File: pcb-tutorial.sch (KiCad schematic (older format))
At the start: 14 parts

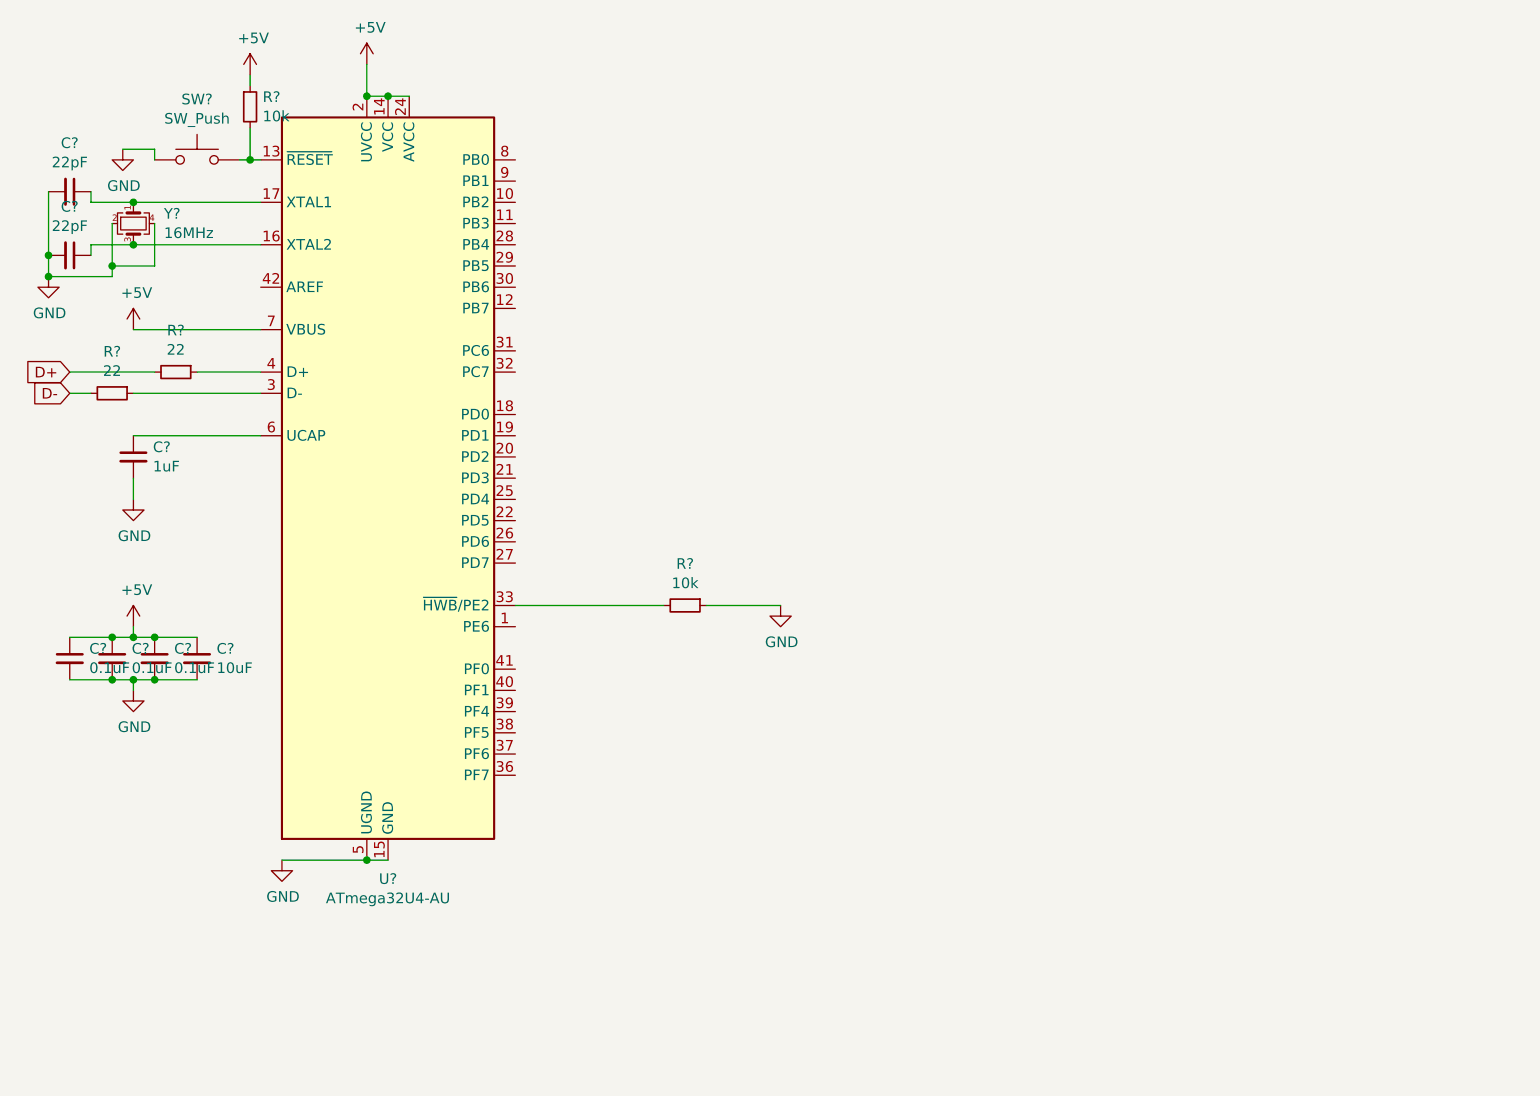
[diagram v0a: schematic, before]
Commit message: completed pcb binding
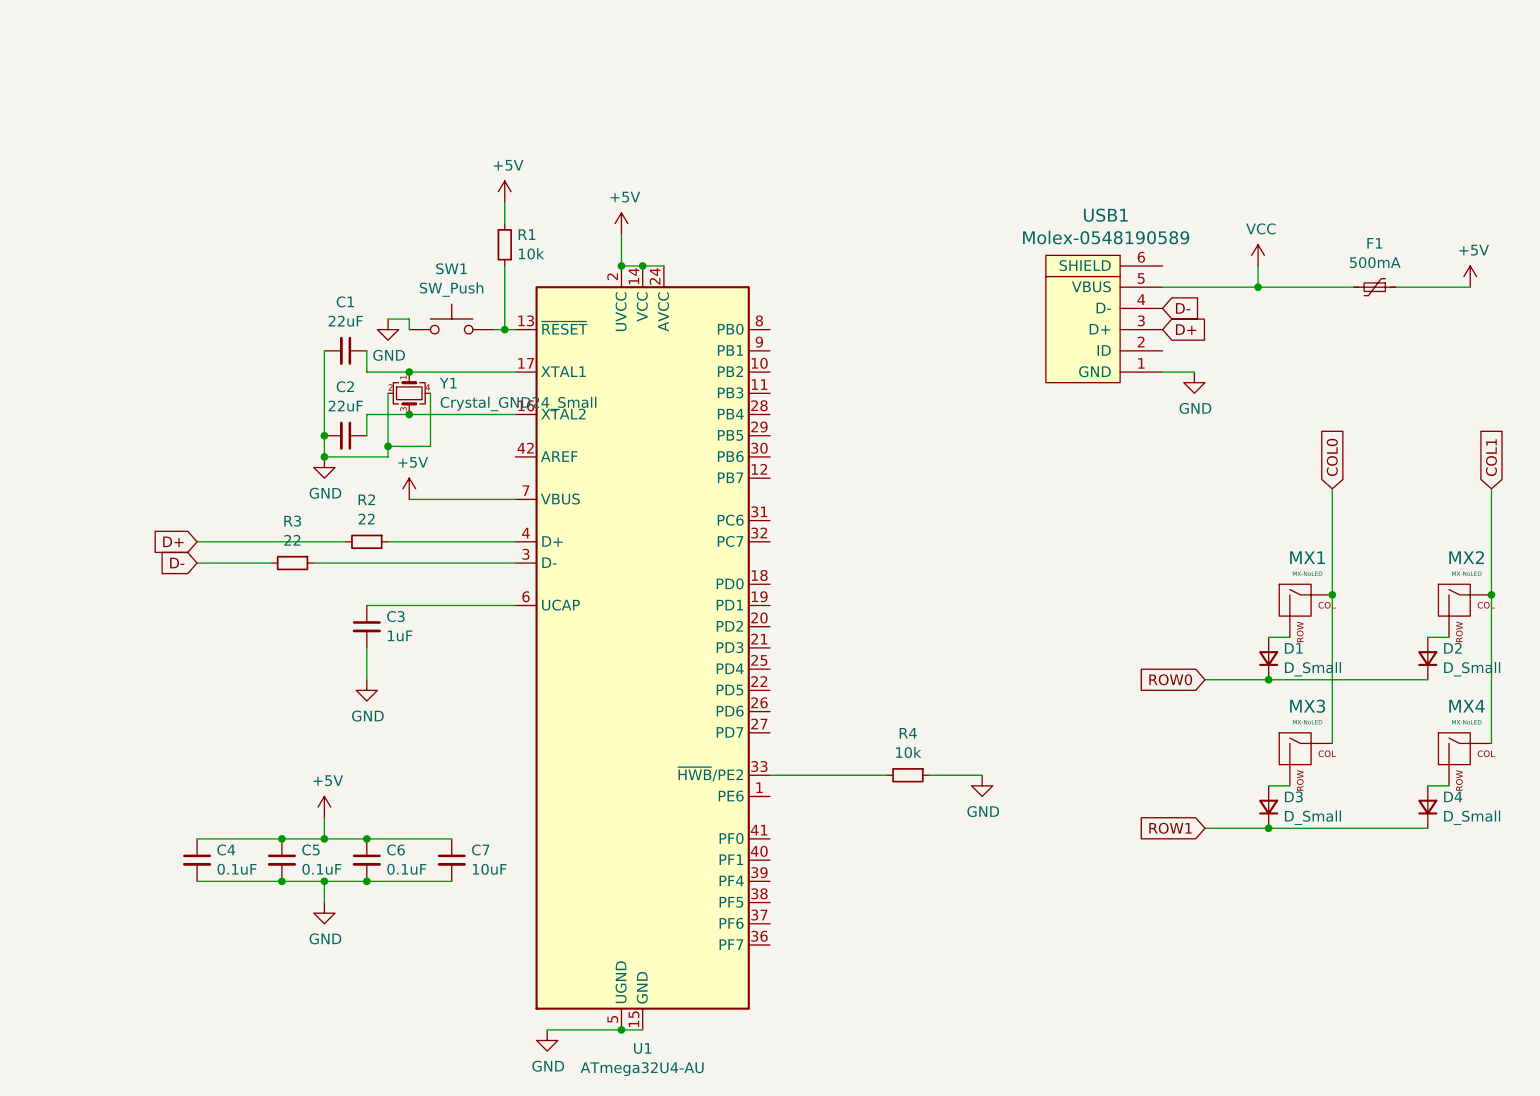
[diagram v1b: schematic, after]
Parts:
- removed C?: 1uF, symbol Device:C_Small
- removed C? (x3): 0.1uF, symbol Device:C_Small
- removed C?: 10uF, symbol Device:C_Small
- removed C? (x2): 22pF, symbol Device:C_Small
- removed R? (x2): 10k, symbol Device:R_Small
- removed R? (x2): 22, symbol Device:R_Small
- removed SW?: SW_Push, symbol Switch:SW_Push
- removed U?: ATmega32U4-AU, Package_QFP:TQFP-44_10x10mm_P0.8mm, symbol MCU_Microchip_ATmega:ATmega32U4-AU
- removed Y?: 16MHz, symbol Device:Crystal_GND24_Small
- added C1, C2: 22uF, Capacitor_SMD:C_0805_2012Metric, symbol Device:C_Small
- added C3: 1uF, Capacitor_SMD:C_0805_2012Metric, symbol Device:C_Small
- added C4, C5, C6: 0.1uF, Capacitor_SMD:C_0805_2012Metric, symbol Device:C_Small
- added C7: 10uF, Capacitor_SMD:C_0805_2012Metric, symbol Device:C_Small
- added D1, D2, D3, D4: D_Small, Diode_SMD:D_SOD-123, symbol Device:D_Small
- added F1: 500mA, Fuse:Fuse_1206_3216Metric, symbol Device:Polyfuse_Small
- added MX1, MX2, MX3, MX4: MX-NoLED, MX_Alps_Hybrid:MX-1U-NoLED, symbol MX_Alps_Hybrid:MX-NoLED
- added R1, R4: 10k, Resistor_SMD:R_0805_2012Metric, symbol Device:R_Small
- added R2, R3: 22, Resistor_SMD:R_0805_2012Metric, symbol Device:R_Small
- added SW1: SW_Push, random-keyboard-parts:SKQG-1155865, symbol Switch:SW_Push
- added U1: ATmega32U4-AU, Package_QFP:TQFP-44_10x10mm_P0.8mm, symbol MCU_Microchip_ATmega:ATmega32U4-AU
- added USB1: Molex-0548190589, random-keyboard-parts:Molex-0548190589, symbol random-keyboard-parts:Molex-0548190589
- added Y1: Crystal_GND24_Small, Crystal:Crystal_SMD_3225-4Pin_3.2x2.5mm, symbol Device:Crystal_GND24_Small
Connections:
- net +5V: now also C4.1, C5.1, C6.1, C7.1, F1.1, R1.2, U1.14 (VCC), U1.2 (UVCC), U1.24 (AVCC), U1.34 (VCC), U1.44 (AVCC), U1.7 (VBUS)
- net D+: now also R2.2, USB1.3 (D+)
- net D-: now also R3.2, USB1.4 (D-)
- net GND: now also C1.2, C2.2, C3.2, C4.2, C5.2, C6.2, C7.2, R4.1, SW1.1, U1.15 (GND), U1.23 (GND), U1.35 (GND), U1.43 (GND), U1.5 (UGND), USB1.1 (GND), Y1.2, Y1.4
- new net: R1.1, SW1.2, U1.13 (~RESET)
- new net: C2.1, U1.16 (XTAL2), Y1.3
- new net: C1.1, U1.17 (XTAL1), Y1.1
- new net: R3.1, U1.3 (D-)
- new net: R4.2, U1.33 (~HWB~/PE2)
- new net: R2.1, U1.4 (D+)
- new net: C3.1, U1.6 (UCAP)
- new net: D1.2 (A), MX1.2 (ROW)
- new net: D2.2 (A), MX2.2 (ROW)
- new net: D3.2 (A), MX3.2 (ROW)
- new net: D4.2 (A), MX4.2 (ROW)
- new net COL0: MX1.1 (COL), MX3.1 (COL)
- new net COL1: MX2.1 (COL), MX4.1 (COL)
- new net ROW0: D1.1 (K), D2.1 (K)
- new net ROW1: D3.1 (K), D4.1 (K)
- new net VCC: F1.2, USB1.5 (VBUS)

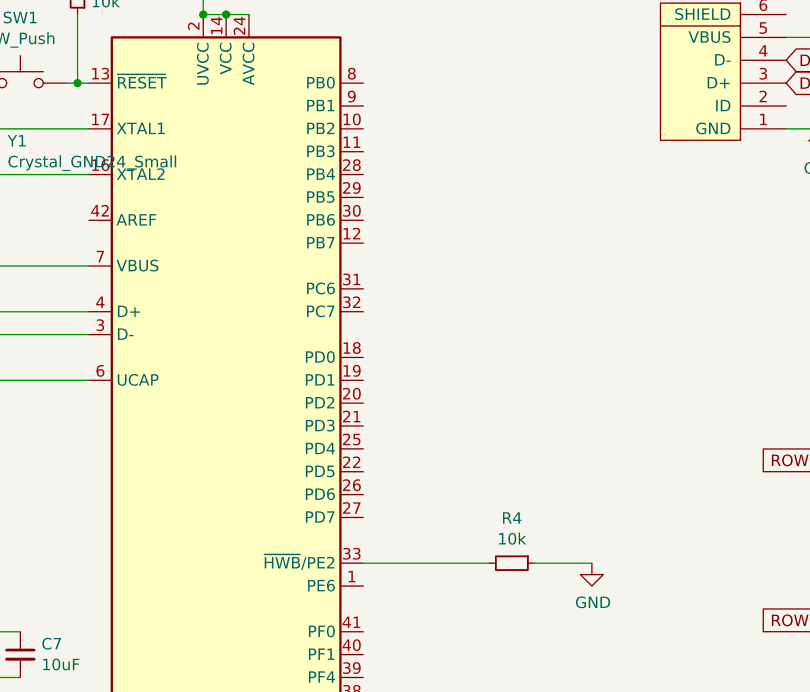
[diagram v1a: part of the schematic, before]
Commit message: Completed PCB Routing
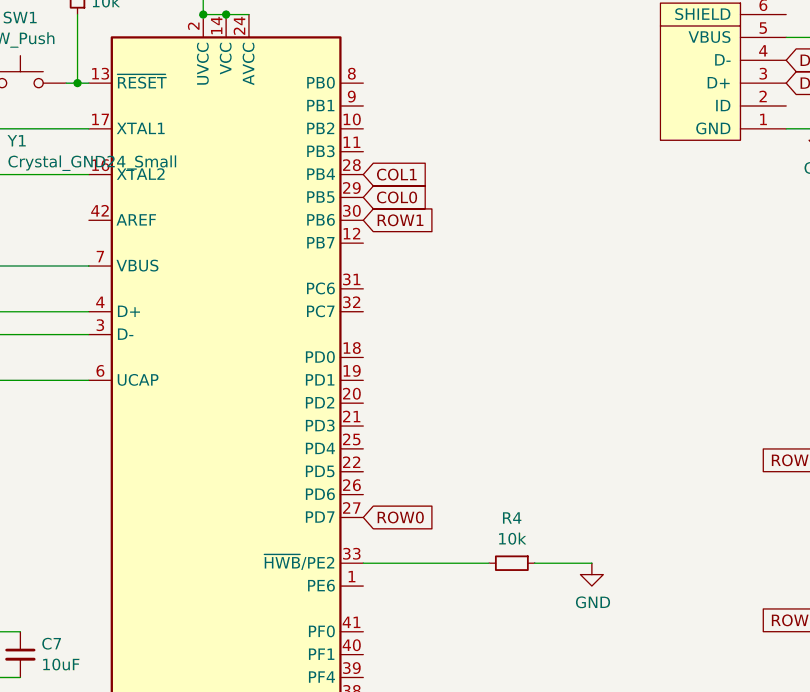
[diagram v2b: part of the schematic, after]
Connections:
- net COL0: now also U1.29 (PB5)
- net COL1: now also U1.28 (PB4)
- net ROW0: now also U1.27 (PD7)
- net ROW1: now also U1.30 (PB6)
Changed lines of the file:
@@
 Text GLabel 6050 4400 0    50   Input ~ 0
 ROW1
+Text GLabel 4000 2550 2    50   Input ~ 0
+COL0
+Text GLabel 4000 2450 2    50   Input ~ 0
+COL1
+Text GLabel 4000 2650 2    50   Input ~ 0
+ROW1
+Text GLabel 4000 3950 2    50   Input ~ 0
+ROW0
 $EndSCHEMATC
